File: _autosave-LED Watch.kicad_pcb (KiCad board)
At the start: 2 copper layers, 41.9 x 49.3 mm, 140 parts, among them J1 AVR-ISP-6, J2 Lipo, J3 Coin Cell, SW1 SW_DPST, SW2 SW_DPST, U10 B39D3RGB-F6C0001HOU1930, U100 B39D3RGB-F6C0001HOU1930, U101 B39D3RGB-F6C0001HOU1930, U102 B39D3RGB-F6C0001HOU1930, U103 B39D3RGB-F6C0001HOU1930, U104 B39D3RGB-F6C0001HOU1930, U105 B39D3RGB-F6C0001HOU1930, U106 B39D3RGB-F6C0001HOU1930, U107 B39D3RGB-F6C0001HOU1930, U108 B39D3RGB-F6C0001HOU1930, U109 B39D3RGB-F6C0001HOU1930, U11 B39D3RGB-F6C0001HOU1930, U110 B39D3RGB-F6C0001HOU1930, U111 B39D3RGB-F6C0001HOU1930, U112 B39D3RGB-F6C0001HOU1930, U113 B39D3RGB-F6C0001HOU1930, U114 B39D3RGB-F6C0001HOU1930, U115 B39D3RGB-F6C0001HOU1930, U116 B39D3RGB-F6C0001HOU1930, U117 B39D3RGB-F6C0001HOU1930, U118 B39D3RGB-F6C0001HOU1930, U119 B39D3RGB-F6C0001HOU1930, U12 B39D3RGB-F6C0001HOU1930, U120 B39D3RGB-F6C0001HOU1930, U121 B39D3RGB-F6C0001HOU1930, U122 B39D3RGB-F6C0001HOU1930, U123 B39D3RGB-F6C0001HOU1930, U124 B39D3RGB-F6C0001HOU1930, U125 B39D3RGB-F6C0001HOU1930, U126 B39D3RGB-F6C0001HOU1930, U127 B39D3RGB-F6C0001HOU1930, U128 B39D3RGB-F6C0001HOU1930, U129 B39D3RGB-F6C0001HOU1930, U13 B39D3RGB-F6C0001HOU1930, U130 B39D3RGB-F6C0001HOU1930, U131 B39D3RGB-F6C0001HOU1930, U132 B39D3RGB-F6C0001HOU1930, U133 B39D3RGB-F6C0001HOU1930, U134 BMI160, U135 ATmega165PA-M, U14 B39D3RGB-F6C0001HOU1930, U15 B39D3RGB-F6C0001HOU1930, U16 B39D3RGB-F6C0001HOU1930, U17 B39D3RGB-F6C0001HOU1930, U18 B39D3RGB-F6C0001HOU1930, U19 B39D3RGB-F6C0001HOU1930, U2 B39D3RGB-F6C0001HOU1930, U20 B39D3RGB-F6C0001HOU1930, U21 B39D3RGB-F6C0001HOU1930, U22 B39D3RGB-F6C0001HOU1930, U23 B39D3RGB-F6C0001HOU1930, U24 B39D3RGB-F6C0001HOU1930, U25 B39D3RGB-F6C0001HOU1930, U26 B39D3RGB-F6C0001HOU1930, U27 B39D3RGB-F6C0001HOU1930, U28 B39D3RGB-F6C0001HOU1930, U29 B39D3RGB-F6C0001HOU1930, U3 B39D3RGB-F6C0001HOU1930, U30 B39D3RGB-F6C0001HOU1930, U31 B39D3RGB-F6C0001HOU1930, U32 B39D3RGB-F6C0001HOU1930, U33 B39D3RGB-F6C0001HOU1930, U34 B39D3RGB-F6C0001HOU1930, U35 B39D3RGB-F6C0001HOU1930, U36 B39D3RGB-F6C0001HOU1930, U37 B39D3RGB-F6C0001HOU1930, U38 B39D3RGB-F6C0001HOU1930, U39 B39D3RGB-F6C0001HOU1930, U4 B39D3RGB-F6C0001HOU1930, U40 B39D3RGB-F6C0001HOU1930, U41 B39D3RGB-F6C0001HOU1930, U42 B39D3RGB-F6C0001HOU1930, U43 B39D3RGB-F6C0001HOU1930, U44 B39D3RGB-F6C0001HOU1930, U45 B39D3RGB-F6C0001HOU1930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

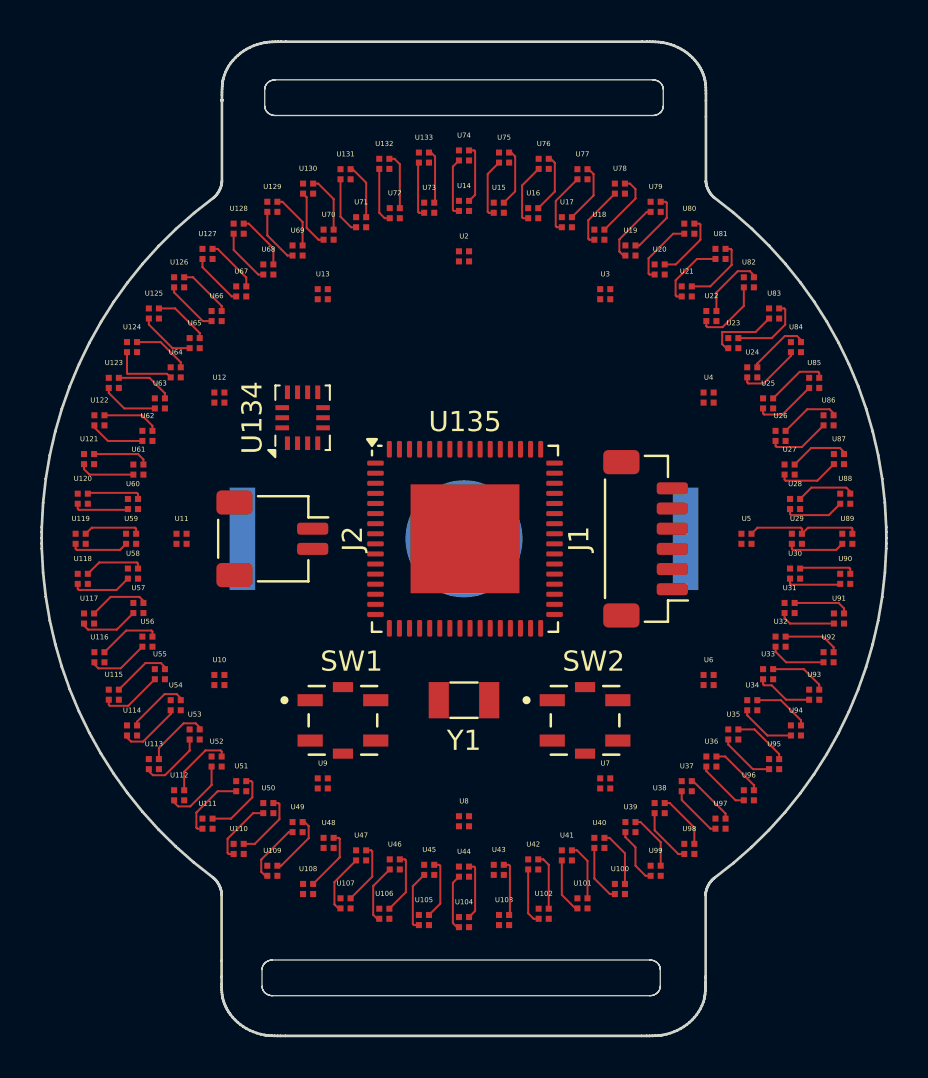
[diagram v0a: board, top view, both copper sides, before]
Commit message: adjusted clocking and spacings.. ready for routing again
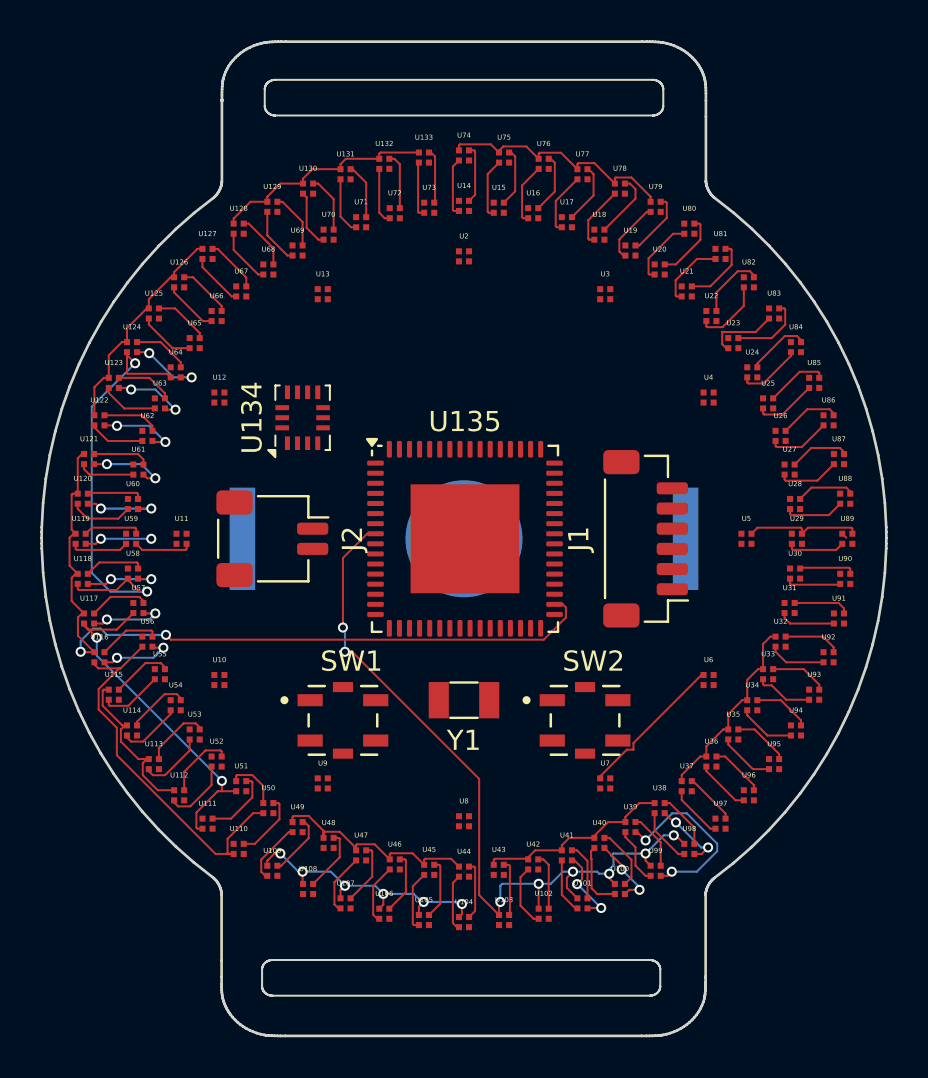
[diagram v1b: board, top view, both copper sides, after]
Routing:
- net /Second5: track 0.00 -> 39.9 mm, vias 0 -> 8
- net /Second8: track 0.00 -> 39.0 mm, vias 0 -> 2
- net /B3: track 30.7 -> 47.6 mm, vias 0 -> 2
- net /G2: track 0.00 -> 16.7 mm, vias 0 -> 6
- net /Second6: track 0.00 -> 14.7 mm, vias 0 -> 6
- net /B1: track 29.7 -> 42.6 mm
- net /Second1: track 0.00 -> 12.6 mm
- net /G1: track 0.00 -> 11.5 mm, vias 0 -> 6
- net /Minute6: track 0.00 -> 11.4 mm
- net /Second10: track 0.00 -> 11.4 mm
- net /G3: track 0.00 -> 11.3 mm, vias 0 -> 6
- net /B2: track 30.3 -> 41.5 mm, vias 0 -> 2
- net /Second9: track 0.00 -> 11.1 mm
- net /G4: track 0.00 -> 10.2 mm, vias 0 -> 4
- net /Minute4: track 0.00 -> 9.85 mm
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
